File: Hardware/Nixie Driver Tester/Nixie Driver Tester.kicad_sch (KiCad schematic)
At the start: 0 parts

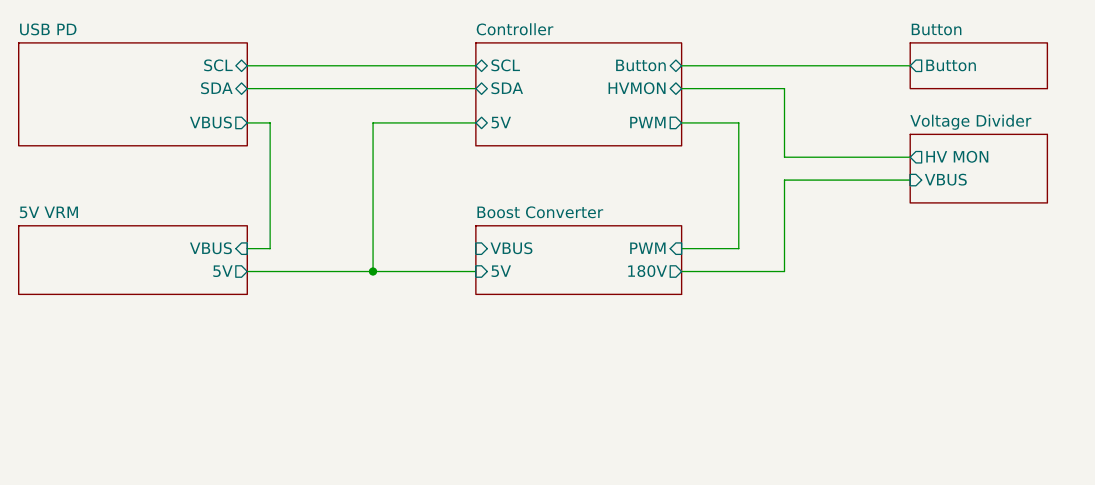
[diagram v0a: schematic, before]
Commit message: Added Nixie headers
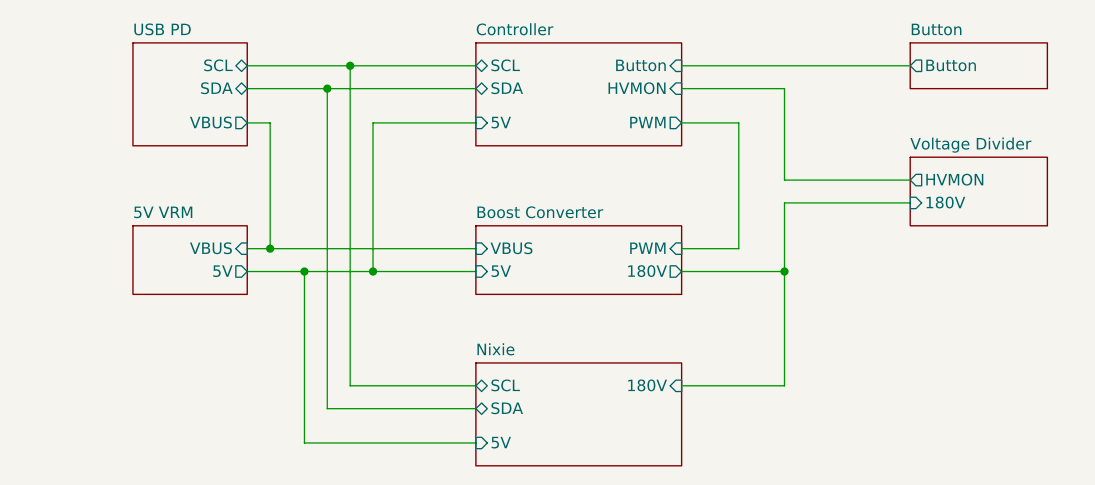
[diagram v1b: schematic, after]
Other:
- added sheet Nixie (Nixie.kicad_sch)
- sheet Voltage Divider ports: added 180V, HVMON; removed HV MON, VBUS

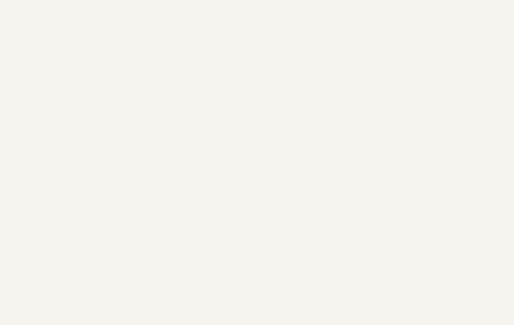
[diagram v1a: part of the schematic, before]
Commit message: One mounting hole
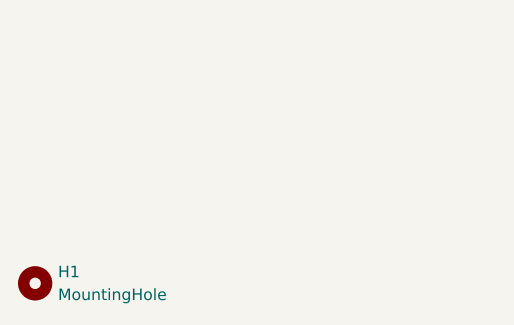
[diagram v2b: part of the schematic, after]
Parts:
- added H1: MountingHole, MountingHole:MountingHole_3.2mm_M3, symbol Mechanical:MountingHole
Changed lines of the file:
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@@
+		)
+	)
+	(symbol
+		(lib_id "Mechanical:MountingHole")
+		(at 27.94 172.72 0)
+		(unit 1)
+		(exclude_from_sim yes)
+		(in_bom no)
+		(on_board yes)
+		(dnp no)
+		(fields_autoplaced yes)
+		(property "Reference" "H1"
+			(at 30.48 171.4499 0)
+			(effects
+				(font
+					(size 1.27 1.27)
+				)
+				(justify left)
+			)
+		)
+		(property "Value" "MountingHole"
+			(at 30.48 173.9899 0)
+			(effects
+				(font
+					(size 1.27 1.27)
+				)
+				(justify left)
+			)
+		)
+		(property "Footprint" "MountingHole:MountingHole_3.2mm_M3"
+			(at 27.94 172.72 0)
+			(effects
+				(font
+					(size 1.27 1.27)
+				)
+				(hide yes)
+			)
+		)
+		(property "Datasheet" "~"
+			(at 27.94 172.72 0)
+			(effects
+				(font
+					(size 1.27 1.27)
+				)
+				(hide yes)
+			)
+		)
+		(property "Description" "Mounting Hole without connection"
+			(at 27.94 172.72 0)
+			(effects
+				(font
+					(size 1.27 1.27)
+				)
+				(hide yes)
+			)
+		)
+		(instances
+			(project ""
+				(path "/c2082ee6-4c2e-4b3c-b2d7-410eae192cfe"
+					(reference "H1")
+					(unit 1)
+				)
+			)
 		)
 	)

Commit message: Two mounting holes
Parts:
- added H2: MountingHole, MountingHole:MountingHole_3.2mm_M3, symbol Mechanical:MountingHole
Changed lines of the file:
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@@
+		)
+	)
+	(symbol
+		(lib_id "Mechanical:MountingHole")
+		(at 27.94 179.07 0)
+		(unit 1)
+		(exclude_from_sim yes)
+		(in_bom no)
+		(on_board yes)
+		(dnp no)
+		(fields_autoplaced yes)
+		(property "Reference" "H2"
+			(at 30.48 177.7999 0)
+			(effects
+				(font
+					(size 1.27 1.27)
+				)
+				(justify left)
+			)
+		)
+		(property "Value" "MountingHole"
+			(at 30.48 180.3399 0)
+			(effects
+				(font
+					(size 1.27 1.27)
+				)
+				(justify left)
+			)
+		)
+		(property "Footprint" "MountingHole:MountingHole_3.2mm_M3"
+			(at 27.94 179.07 0)
+			(effects
+				(font
+					(size 1.27 1.27)
+				)
+				(hide yes)
+			)
+		)
+		(property "Datasheet" "~"
+			(at 27.94 179.07 0)
+			(effects
+				(font
+					(size 1.27 1.27)
+				)
+				(hide yes)
+			)
+		)
+		(property "Description" "Mounting Hole without connection"
+			(at 27.94 179.07 0)
+			(effects
+				(font
+					(size 1.27 1.27)
+				)
+				(hide yes)
+			)
+		)
+		(instances
+			(project "Nixie Driver Tester"
+				(path "/c2082ee6-4c2e-4b3c-b2d7-410eae192cfe"
+					(reference "H2")
+					(unit 1)
+				)
+			)
 		)
 	)

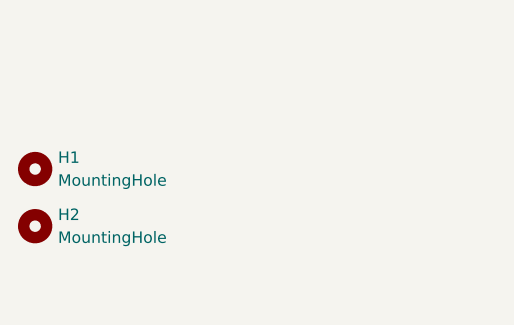
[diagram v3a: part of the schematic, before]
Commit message: Major layout change to get the L out of the way
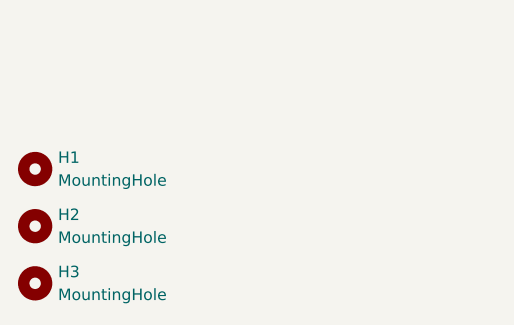
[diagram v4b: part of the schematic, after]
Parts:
- added H3: MountingHole, MountingHole:MountingHole_3.2mm_M3, symbol Mechanical:MountingHole
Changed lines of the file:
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@@
+	(symbol
+		(lib_id "Mechanical:MountingHole")
+		(at 27.94 185.42 0)
+		(unit 1)
+		(exclude_from_sim yes)
+		(in_bom no)
+		(on_board yes)
+		(dnp no)
+		(fields_autoplaced yes)
+		(property "Reference" "H3"
+			(at 30.48 184.1499 0)
+			(effects
+				(font
+					(size 1.27 1.27)
+				)
+				(justify left)
+			)
+		)
+		(property "Value" "MountingHole"
+			(at 30.48 186.6899 0)
+			(effects
+				(font
+					(size 1.27 1.27)
+				)
+				(justify left)
+			)
+		)
+		(property "Footprint" "MountingHole:MountingHole_3.2mm_M3"
+			(at 27.94 185.42 0)
+			(effects
+				(font
+					(size 1.27 1.27)
+				)
+				(hide yes)
+			)
+		)
+		(property "Datasheet" "~"
+			(at 27.94 185.42 0)
+			(effects
+				(font
+					(size 1.27 1.27)
+				)
+				(hide yes)
+			)
+		)
+		(property "Description" "Mounting Hole without connection"
+			(at 27.94 185.42 0)
+			(effects
+				(font
+					(size 1.27 1.27)
+				)
+				(hide yes)
+			)
+		)
+		(instances
+			(project "Nixie Driver Tester"
+				(path "/c2082ee6-4c2e-4b3c-b2d7-410eae192cfe"
+					(reference "H3")
+					(unit 1)
+				)
+			)
+		)
+	)
 	(symbol
 		(lib_id "Mechanical:MountingHole")

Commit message: Replace OLED mounting hole with slot
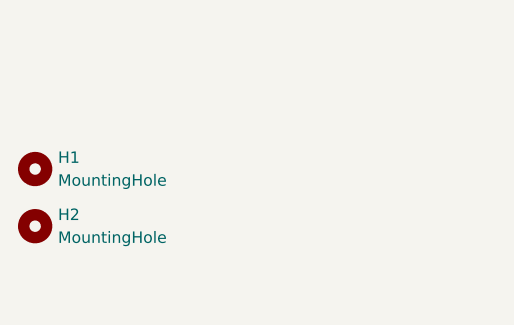
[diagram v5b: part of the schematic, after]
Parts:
- removed H3: MountingHole, MountingHole:MountingHole_3.2mm_M3, symbol Mechanical:MountingHole
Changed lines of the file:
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@@
-	(symbol
-		(lib_id "Mechanical:MountingHole")
-		(at 27.94 185.42 0)
-		(unit 1)
-		(exclude_from_sim yes)
-		(in_bom no)
-		(on_board yes)
-		(dnp no)
-		(fields_autoplaced yes)
-		(property "Reference" "H3"
-			(at 30.48 184.1499 0)
-			(effects
-				(font
-					(size 1.27 1.27)
-				)
-				(justify left)
-			)
-		)
-		(property "Value" "MountingHole"
-			(at 30.48 186.6899 0)
-			(effects
-				(font
-					(size 1.27 1.27)
-				)
-				(justify left)
-			)
-		)
-		(property "Footprint" "MountingHole:MountingHole_3.2mm_M3"
-			(at 27.94 185.42 0)
-			(effects
-				(font
-					(size 1.27 1.27)
-				)
-				(hide yes)
-			)
-		)
-		(property "Datasheet" "~"
-			(at 27.94 185.42 0)
-			(effects
-				(font
-					(size 1.27 1.27)
-				)
-				(hide yes)
-			)
-		)
-		(property "Description" "Mounting Hole without connection"
-			(at 27.94 185.42 0)
-			(effects
-				(font
-					(size 1.27 1.27)
-				)
-				(hide yes)
-			)
-		)
-		(instances
-			(project "Nixie Driver Tester"
-				(path "/c2082ee6-4c2e-4b3c-b2d7-410eae192cfe"
-					(reference "H3")
-					(unit 1)
-				)
-			)
-		)
-	)
 	(symbol
 		(lib_id "Mechanical:MountingHole")
